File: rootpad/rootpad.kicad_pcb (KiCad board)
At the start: 2 copper layers, 77.8 x 110.3 mm, 56 parts, among them J1 USB_B_Mini, SW1 SW_Push, U1 ATmega32U4-AU, Y1 16MHz

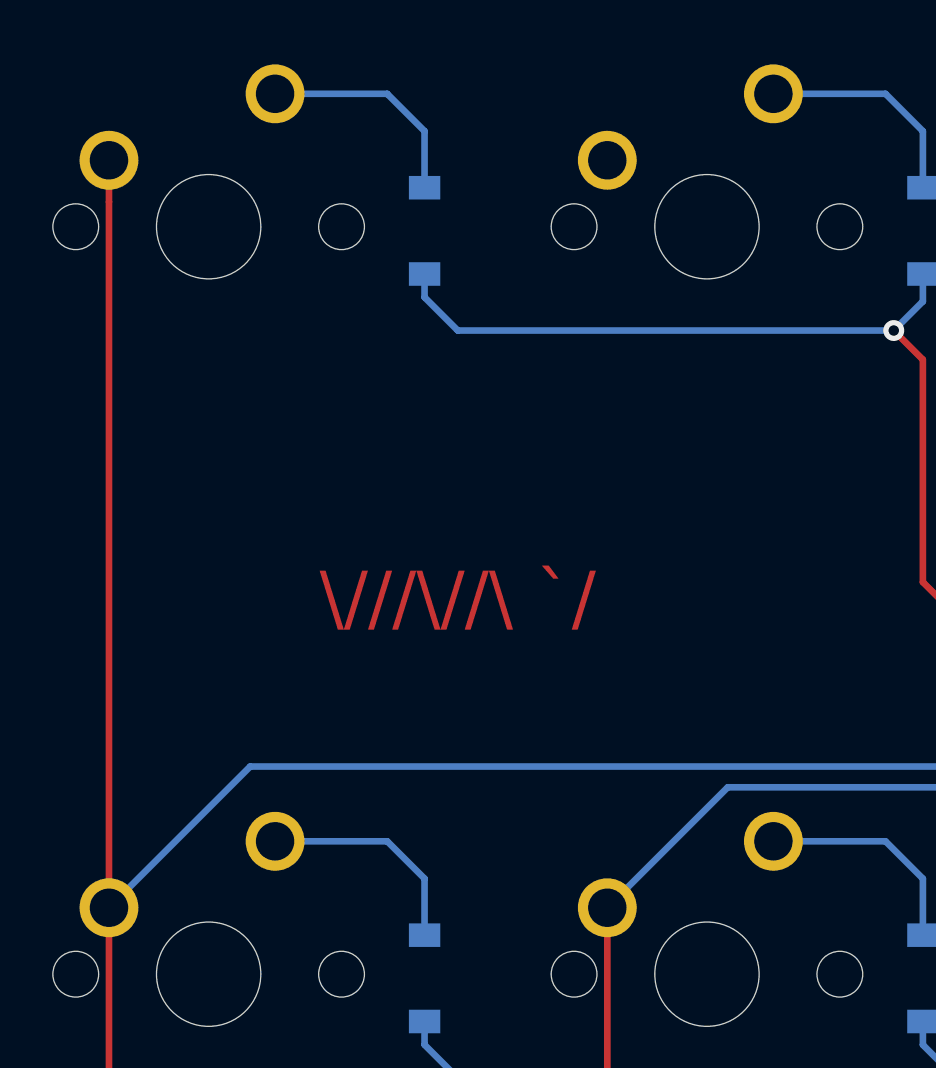
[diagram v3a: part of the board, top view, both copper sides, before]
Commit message: Cleared area for name and moved some silkscreen labels
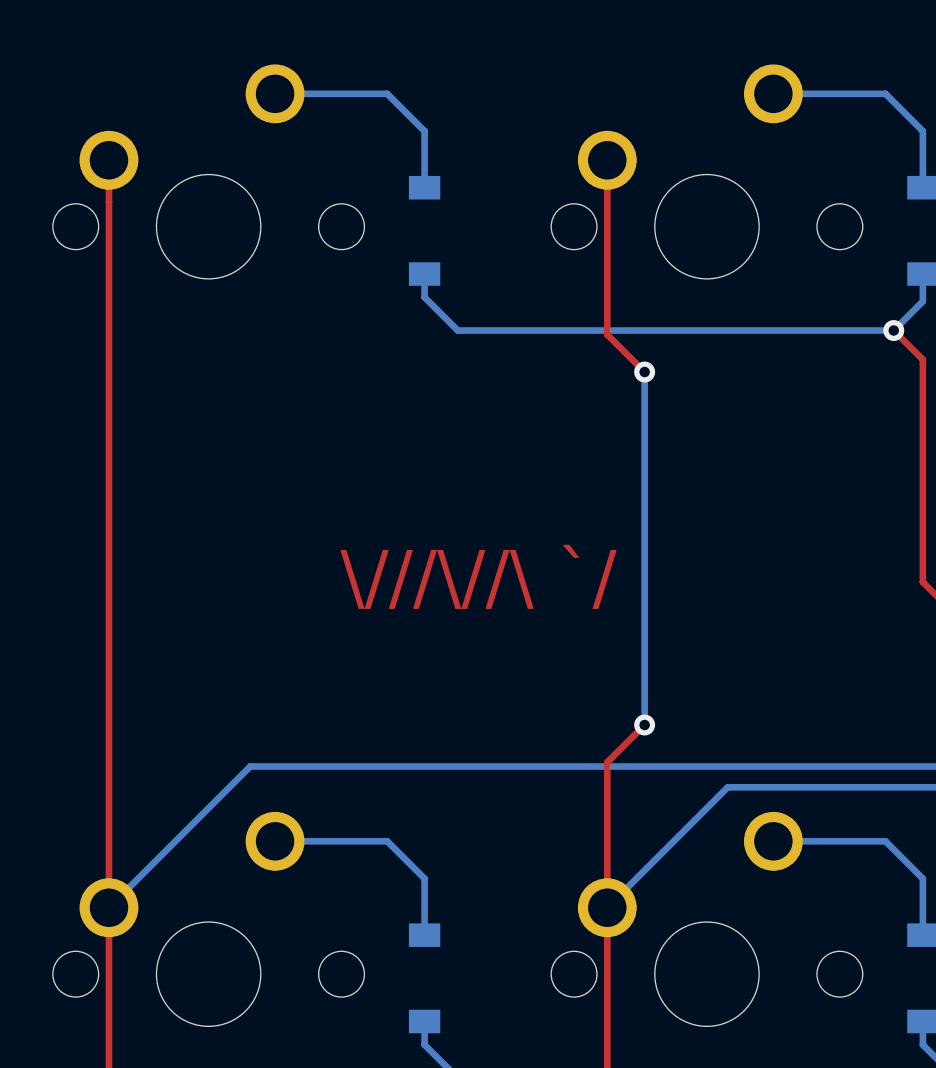
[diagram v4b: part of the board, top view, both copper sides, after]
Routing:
- net COL1: track 96.5 -> 126.2 mm, vias 1 -> 3
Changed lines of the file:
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@@
-(kicad_pcb (version 20171130) (host pcbnew 5.1.4)
+(kicad_pcb (version 20171130) (host pcbnew "(5.1.2)-2")
   (general
     (thickness 1.6)
     (drawings 10)
-    (tracks 397)
+    (tracks 404)
     (zones 0)
     (modules 56)
@@
     (tags SOD-123)
     (attr smd)
-    (fp_text reference D18 (at 0 2 90) (layer B.SilkS)
+    (fp_text reference D18 (at 4.12877 -0.0675 90) (layer B.SilkS)
       (effects (font (size 1 1) (thickness 0.15)) (justify mirror))
     )
@@
       (effects (font (size 1 1) (thickness 0.15)) (justify mirror))
     )
-    (fp_text user %R (at 0 2 90) (layer B.Fab)
+    (fp_text user %R (at 4.12877 -0.0675 90) (layer B.Fab)
       (effects (font (size 1 1) (thickness 0.15)) (justify mirror))
     )
@@
     (tags SOD-123)
     (attr smd)
-    (fp_text reference D14 (at 0 2 90) (layer B.SilkS)
+    (fp_text reference D14 (at 4.12877 -0.0675 90) (layer B.SilkS)
       (effects (font (size 1 1) (thickness 0.15)) (justify mirror))
     )
@@
       (effects (font (size 1 1) (thickness 0.15)) (justify mirror))
     )
-    (fp_text user %R (at 0 2 90) (layer B.Fab)
+    (fp_text user %R (at 4.12877 -0.0675 90) (layer B.Fab)
       (effects (font (size 1 1) (thickness 0.15)) (justify mirror))
     )
@@
     (tags SOD-123)
     (attr smd)
-    (fp_text reference D10 (at 0 2 90) (layer B.SilkS)
+    (fp_text reference D10 (at 4.12877 -0.0675 90) (layer B.SilkS)
       (effects (font (size 1 1) (thickness 0.15)) (justify mirror))
     )
@@
       (effects (font (size 1 1) (thickness 0.15)) (justify mirror))
     )
-    (fp_text user %R (at 0 2 90) (layer B.Fab)
+    (fp_text user %R (at 4.12877 -0.0675 90) (layer B.Fab)
       (effects (font (size 1 1) (thickness 0.15)) (justify mirror))
     )
@@
     (tags SOD-123)
     (attr smd)
-    (fp_text reference D6 (at 0 2 90) (layer B.SilkS)
+    (fp_text reference D6 (at 4.12877 -0.0675 90) (layer B.SilkS)
       (effects (font (size 1 1) (thickness 0.15)) (justify mirror))
     )
@@
       (effects (font (size 1 1) (thickness 0.15)) (justify mirror))
     )
-    (fp_text user %R (at 0 2 90) (layer B.Fab)
+    (fp_text user %R (at 4.12877 -0.0675 90) (layer B.Fab)
       (effects (font (size 1 1) (thickness 0.15)) (justify mirror))
     )
@@
     )
   )
-  (gr_text "\\///\\//\\ `/" (at 139.7 74.549) (layer F.Mask)
+  (gr_text "\\///\\//\\ `/" (at 140.49375 73.75525) (layer F.Mask)
     (effects (font (size 2 2) (thickness 0.35)))
   )
-  (gr_text "\\///\\//\\ `/" (at 139.7 74.549) (layer F.Cu)
+  (gr_text "\\///\\//\\ `/" (at 140.49375 73.75525) (layer F.Cu)
     (effects (font (size 2 2) (thickness 0.35)))
   )
@@
   (segment (start 150.02129 81.75625) (end 145.41627 86.36127) (width 0.254) (layer B.Cu) (net 32))
   (segment (start 168.275 81.75625) (end 150.02129 81.75625) (width 0.254) (layer B.Cu) (net 32))
+  (via (at 146.84375 65.88125) (size 0.8) (drill 0.4) (layers F.Cu B.Cu) (net 32))
+  (segment (start 145.41627 57.78627) (end 145.41627 64.45377) (width 0.254) (layer F.Cu) (net 32))
+  (segment (start 145.41627 64.45377) (end 146.84375 65.88125) (width 0.254) (layer F.Cu) (net 32))
+  (via (at 146.84375 79.375) (size 0.8) (drill 0.4) (layers F.Cu B.Cu) (net 32))
+  (segment (start 146.84375 65.88125) (end 146.84375 79.375) (width 0.254) (layer B.Cu) (net 32))
+  (segment (start 145.41627 80.80248) (end 146.84375 79.375) (width 0.254) (layer F.Cu) (net 32))
+  (segment (start 145.41627 86.36127) (end 145.41627 80.80248) (width 0.254) (layer F.Cu) (net 32))
   (segment (start 164.46627 124.46127) (end 164.46627 143.51127) (width 0.254) (layer F.Cu) (net 33))
   (via (at 173.0375 74.6125) (size 0.8) (drill 0.4) (layers F.Cu B.Cu) (net 33))

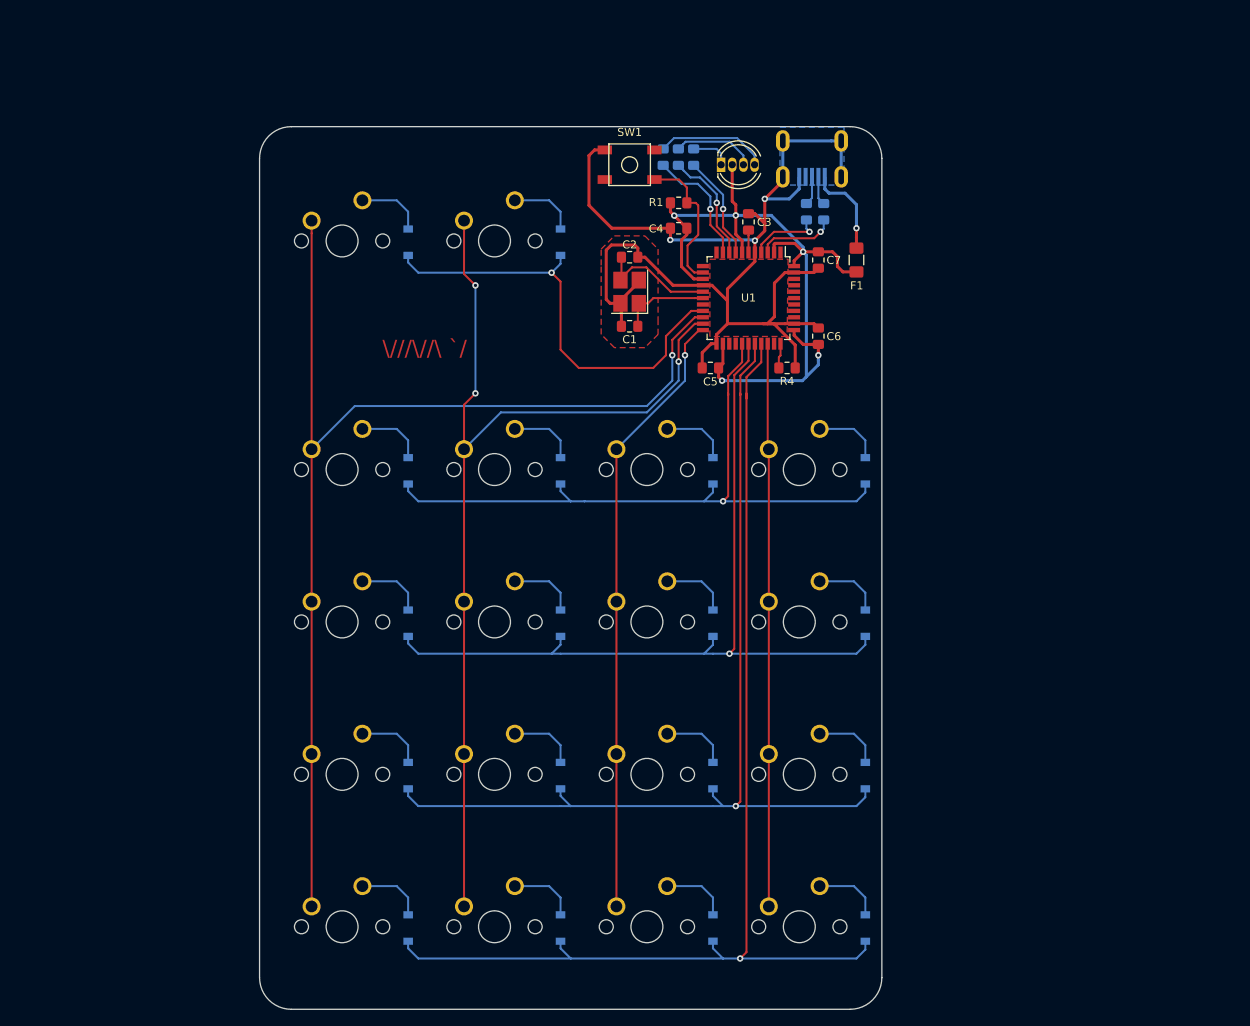
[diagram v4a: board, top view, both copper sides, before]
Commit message: Rearranged switches to fit 100x100 mm pcb
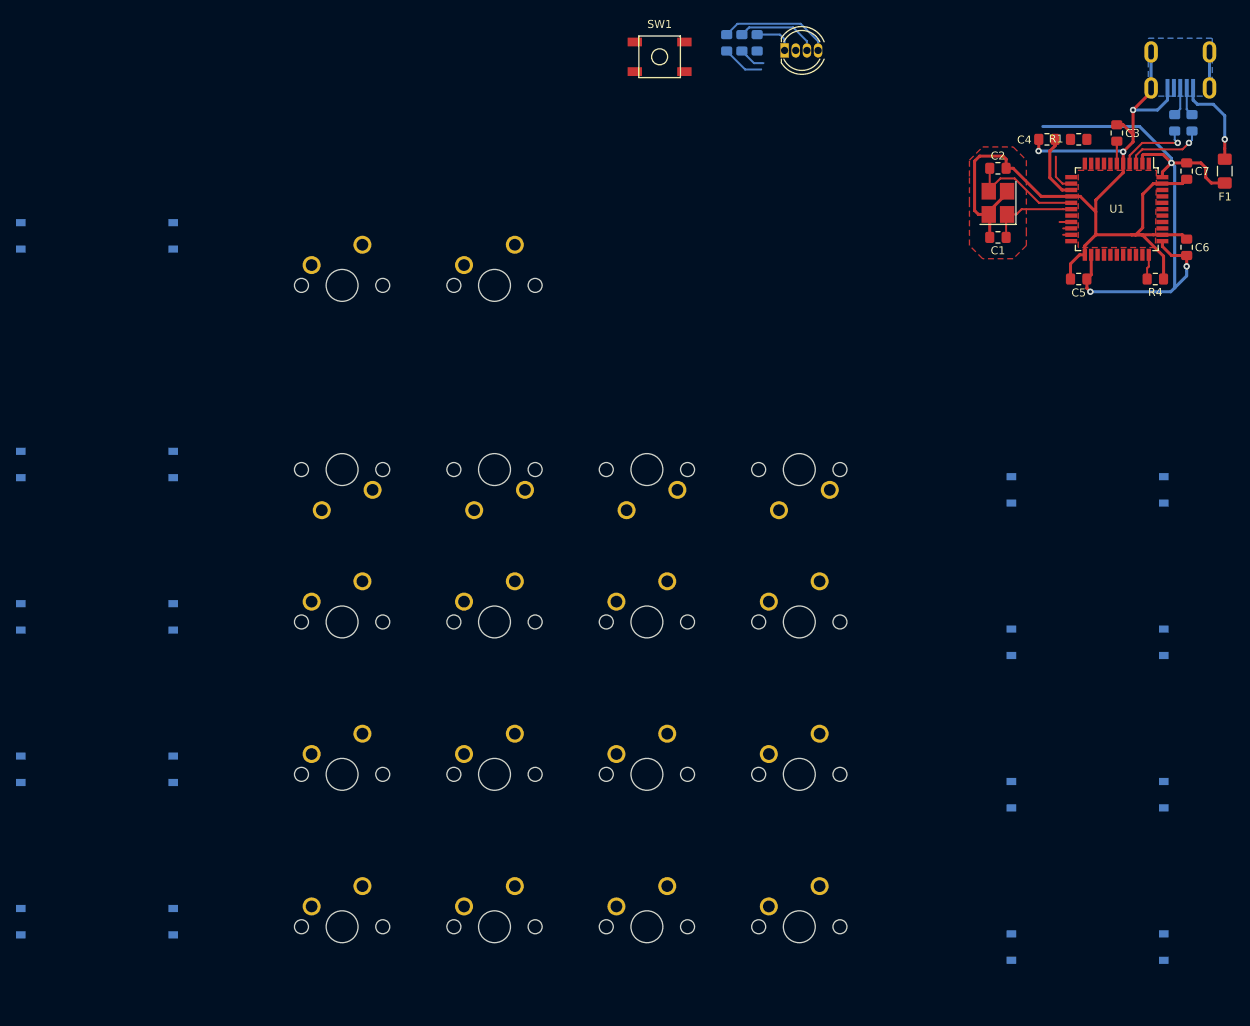
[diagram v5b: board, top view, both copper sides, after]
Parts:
- moved R1 50.6 mm to (222.2, 47.6)
- moved D1 48.4 mm to (90.0, 59.7)
- moved D11 48.4 mm to (90.0, 126.4)
- moved D15 48.4 mm to (90.0, 145.4)
- moved D3 48.4 mm to (90.0, 88.3)
- moved D7 48.4 mm to (90.0, 107.3)
- moved D12 48.4 mm to (109.1, 126.4)
- moved D16 48.4 mm to (109.1, 145.4)
- moved D2 48.4 mm to (109.1, 59.7)
- moved D4 48.4 mm to (109.1, 88.3)
- moved D8 48.4 mm to (109.1, 107.3)
- moved C6 47.4 mm to (235.7, 61.1)
- moved C7 47.4 mm to (235.7, 51.6)
- moved C1 47.4 mm to (212.2, 59.9)
- moved C2 47.4 mm to (212.2, 51.2)
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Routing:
- net ROW4: track 144.0 -> 0.00 mm, vias 1 -> 0
- net COL0: track 144.5 -> 1.00 mm, vias 1 -> 0
- net COL1: track 126.2 -> 1.00 mm, vias 3 -> 0
- net ROW3: track 124.4 -> 0.00 mm, vias 1 -> 0
- net ROW2: track 105.1 -> 0.00 mm, vias 1 -> 0
- net ROW1: track 86.3 -> 0.00 mm, vias 1 -> 0
- net COL2: track 76.8 -> 0.47 mm, vias 1 -> 0
- net COL3: track 70.2 -> 0.00 mm
- net ROW0: track 55.1 -> 1.46 mm, vias 1 -> 0
- net GND: track 150.7 -> 123.5 mm
- net +5V: track 98.5 -> 83.0 mm, vias 5 -> 3
- net Net-(R1-Pad2): track 18.3 -> 4.80 mm
- net LED_R: track 13.1 -> 0.00 mm, vias 1 -> 0
- net LED_G: track 14.2 -> 3.32 mm, vias 1 -> 0
- net LED_B: track 15.2 -> 5.27 mm, vias 1 -> 0
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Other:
- board outline removed
- board text removed: "\///\//\ `/"

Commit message: Routed MCU,XTAL,USB.RST
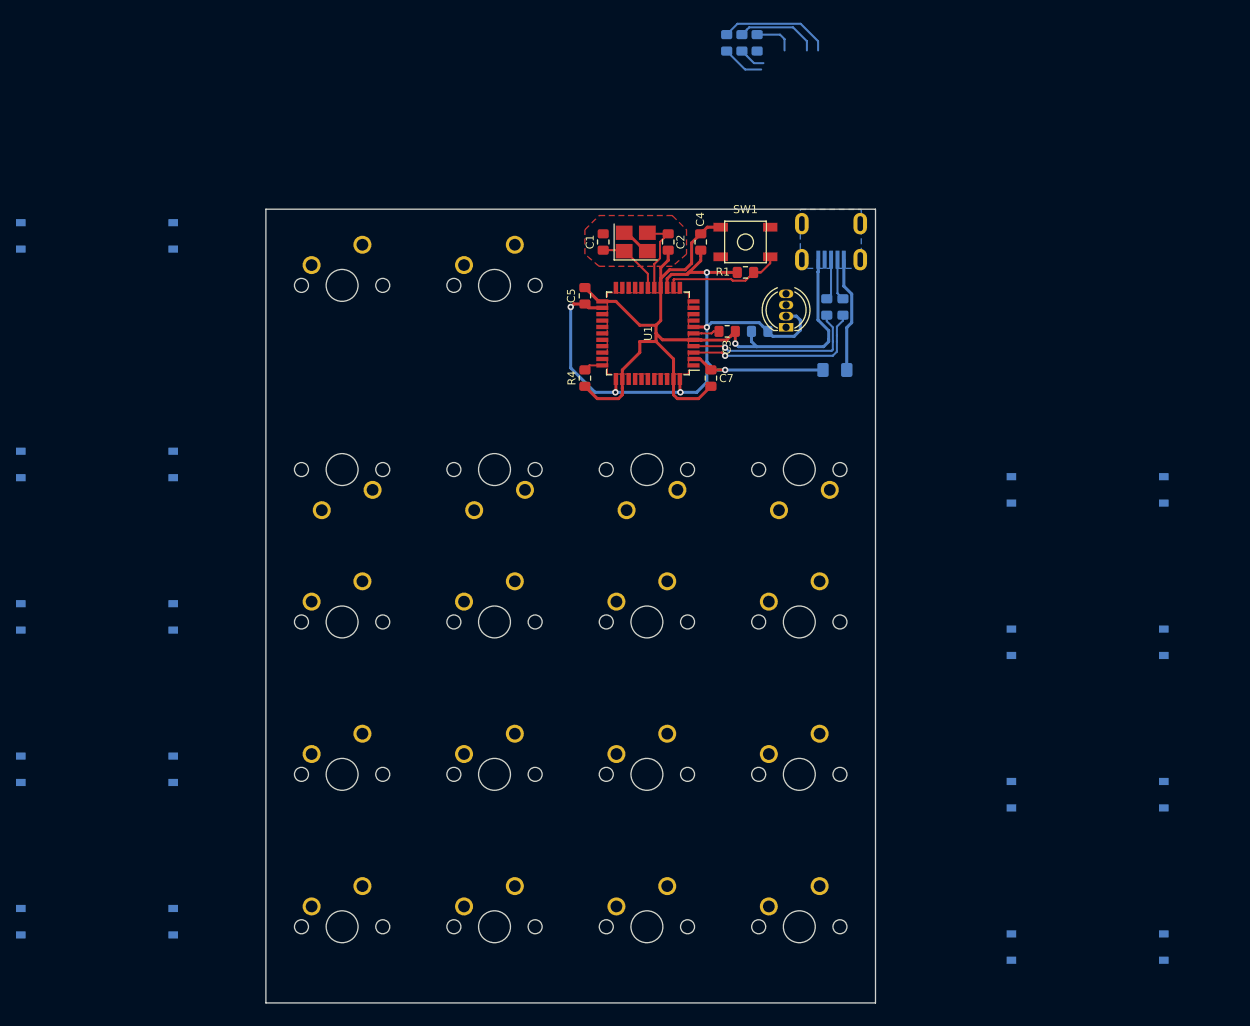
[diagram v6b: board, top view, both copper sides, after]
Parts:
- C6, F1: moved to B.Cu
- moved R4 72.4 mm to (160.5, 77.5), turned to 90 degrees
- moved C7 64.9 mm to (176.3, 77.5)
- moved C5 61.8 mm to (160.5, 67.2), turned to 90 degrees
- moved U1 60.6 mm to (168.4, 71.9), turned to 180 degrees
- moved F1 54.7 mm to (191.8, 76.5), turned to 0 degrees
- moved C3 54.7 mm to (178.3, 71.6), turned to 0 degrees
- moved C6 54.4 mm to (182.4, 71.6), turned to 180 degrees
- moved C1 49.3 mm to (162.8, 60.5), turned to 90 degrees
- moved R3 49.3 mm to (192.8, 68.6)
- moved R2 49.2 mm to (190.8, 68.6)
- moved J1 48.6 mm to (191.3, 58.2)
- moved Y1 45.5 mm to (166.9, 60.5), turned to 0 degrees
- moved C4 45.1 mm to (175.0, 60.5), turned to 90 degrees
- moved R1 44.9 mm to (180.6, 64.3)
- moved C2 42.2 mm to (170.9, 60.5), turned to 90 degrees
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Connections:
- U1 pad 10: LED_B -> Net-(U1-Pad10)
- U1 pad 19: ROW0 -> Net-(U1-Pad19)
- U1 pad 20: COL0 -> Net-(U1-Pad20)
- U1 pad 21: COL1 -> Net-(U1-Pad21)
- U1 pad 22: COL2 -> Net-(U1-Pad22)
- U1 pad 27: ROW1 -> Net-(U1-Pad27)
- U1 pad 28: ROW2 -> Net-(U1-Pad28)
- U1 pad 29: ROW3 -> Net-(U1-Pad29)
- U1 pad 30: ROW4 -> Net-(U1-Pad30)
- U1 pad 31: COL3 -> Net-(U1-Pad31)
- U1 pad 8: LED_R -> Net-(U1-Pad8)
- U1 pad 9: LED_G -> Net-(U1-Pad9)
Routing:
- net GND: track 123.5 -> 105.1 mm, vias 3 -> 1
- net +5V: track 83.0 -> 99.8 mm, vias 3 -> 6
- net Net-(R3-Pad2): track 9.92 -> 23.2 mm
- net Net-(R2-Pad1): track 9.32 -> 22.3 mm
- net Net-(R1-Pad2): track 4.80 -> 14.9 mm
- net Net-(C2-Pad2): track 15.2 -> 10.1 mm
- net VCC: track 11.7 -> 15.3 mm, vias 1 -> 0
- net Net-(C1-Pad1): track 11.2 -> 8.57 mm
- net D-: track 3.61 -> 5.18 mm
- net D+: track 3.62 -> 5.11 mm
- net ROW0: track 1.46 -> 0.00 mm
- net COL1: track 1.00 -> 0.00 mm
- net COL0: track 1.00 -> 0.00 mm
- net Net-(R4-Pad2): track 3.12 -> 2.41 mm
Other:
- board outline added: 76.2 x 99.2 mm
